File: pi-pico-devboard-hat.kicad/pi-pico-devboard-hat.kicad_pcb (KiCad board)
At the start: 2 copper layers, 65 x 56 mm, 6 parts, among them J1 Conn_01x24_Male, P1 Conn_02x20_Odd_Even

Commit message: first prototype DRC error free
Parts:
- added ?: , , F.Cu at (258.2, 126.2)
- added D1: D_Schottky, Diode_THT:D_DO-41_SOD81_P7.62mm_Horizontal, F.Cu at (209.6, 109.5)
- added J2: Conn_Pico_1, Connector_PinHeader_2.54mm:PinHeader_1x20_P2.54mm_Vertical, F.Cu at (202.0, 141.3)
- added J3: Conn_SWD, Connector_PinHeader_2.54mm:PinHeader_1x03_P2.54mm_Vertical, F.Cu at (255.6, 129.4)
- added J4: Conn_Pico_2, Connector_PinHeader_2.54mm:PinHeader_1x20_P2.54mm_Vertical, F.Cu at (250.2, 113.2)
- added SW1: SW_Reset, Button_Switch_THT:SW_PUSH_6mm, F.Cu at (261.7, 110.9)
- added U1: Pico, user:RPi_Pico_SMD_TH, F.Cu at (226.1, 126.9)
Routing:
- net /GPIO15(RXD0): track 8.70 -> 60.4 mm
- net /GPIO14(TXD0): track 8.70 -> 50.8 mm, vias 0 -> 1
- net /GPIO25(GEN6): track 7.39 -> 47.7 mm
- net Net-(J4-Pad10): track 0.00 -> 40.1 mm, vias 0 -> 1
- net /GPIO24(GEN5): track 7.29 -> 45.4 mm
- net +5V: track 2.54 -> 19.6 mm
- net /VSYS: track 0.00 -> 11.4 mm
- net GND: track 10.4 -> 16.1 mm
- net Net-(J2-Pad9): track 0.00 -> 5.56 mm
- net Net-(J2-Pad7): track 0.00 -> 5.56 mm
- net Net-(J2-Pad6): track 0.00 -> 5.56 mm
- net Net-(J2-Pad5): track 0.00 -> 5.56 mm
- net Net-(J2-Pad4): track 0.00 -> 5.56 mm
- net Net-(J2-Pad20): track 0.00 -> 5.56 mm
- net Net-(J2-Pad19): track 0.00 -> 5.56 mm
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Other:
- board text added: "Reset"

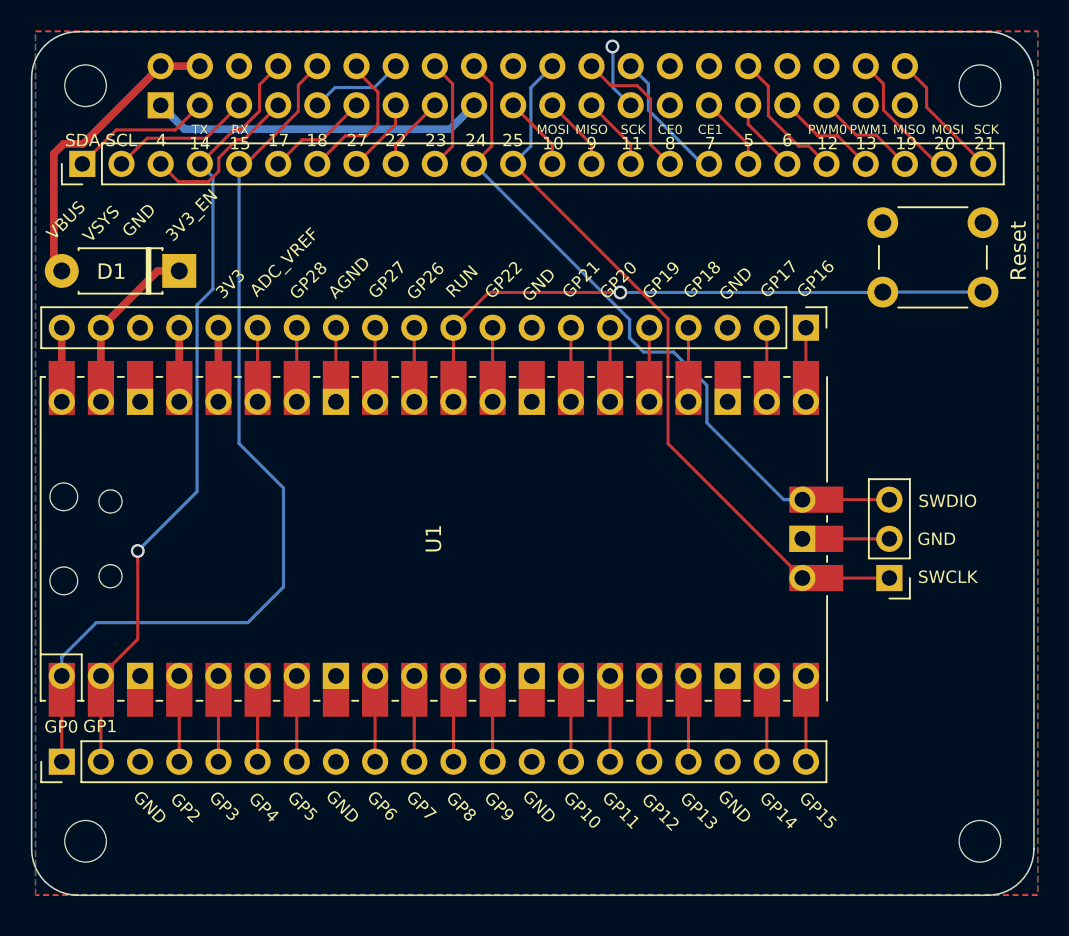
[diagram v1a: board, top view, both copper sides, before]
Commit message: Rev 2: removed unneeded connectors
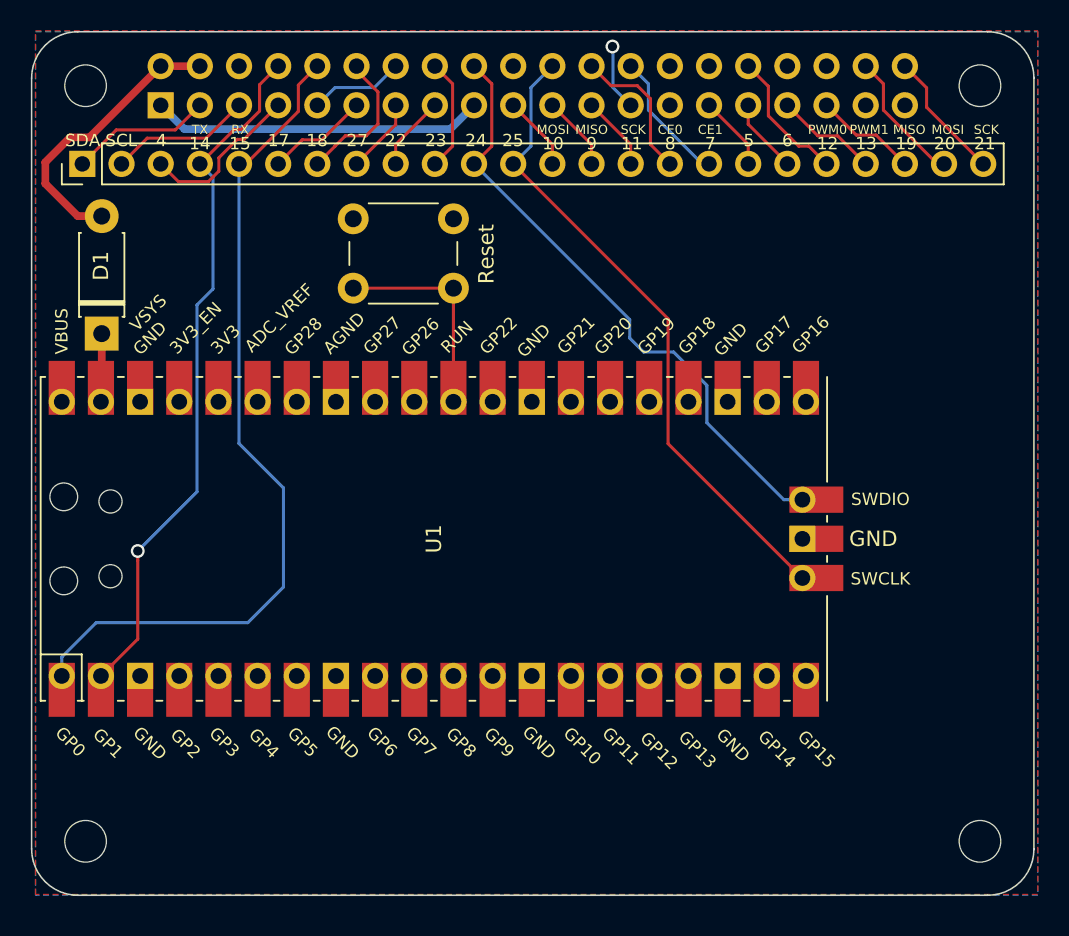
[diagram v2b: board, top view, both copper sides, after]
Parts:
- removed ?: , 
- removed J2: Conn_Pico_1, Connector_PinHeader_2.54mm:PinHeader_1x20_P2.54mm_Vertical
- removed J3: Conn_SWD, Connector_PinHeader_2.54mm:PinHeader_1x03_P2.54mm_Vertical
- removed J4: Conn_Pico_2, Connector_PinHeader_2.54mm:PinHeader_1x20_P2.54mm_Vertical
- moved SW1 34.3 mm to (227.4, 110.6)
- moved D1 6.47 mm to (204.5, 113.6), turned to 90 degrees
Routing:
- net Net-(SW1-Pad1): track 40.1 -> 13.9 mm, vias 1 -> 0
- net /VSYS: track 11.4 -> 4.44 mm
- net /GPIO25(GEN6): track 47.7 -> 42.0 mm
- net /GPIO24(GEN5): track 45.4 -> 39.7 mm
- net GND: track 16.1 -> 10.4 mm
- net Net-(U1-Pad9): track 5.56 -> 0.00 mm
- net Net-(U1-Pad7): track 5.56 -> 0.00 mm
- net Net-(U1-Pad6): track 5.56 -> 0.00 mm
- net Net-(U1-Pad5): track 5.56 -> 0.00 mm
- net Net-(U1-Pad4): track 5.56 -> 0.00 mm
- net Net-(U1-Pad20): track 5.56 -> 0.00 mm
- net Net-(U1-Pad19): track 5.56 -> 0.00 mm
- net Net-(U1-Pad17): track 5.56 -> 0.00 mm
- net Net-(U1-Pad16): track 5.56 -> 0.00 mm
- net Net-(U1-Pad15): track 5.56 -> 0.00 mm
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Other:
- board text added: "GND"
- board text added: "Rev: 2"
- board text added: "https://github.com/bablokb/pi-pico-devboard-hat"

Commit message: Rev 3: added IC-connector with optional pullups
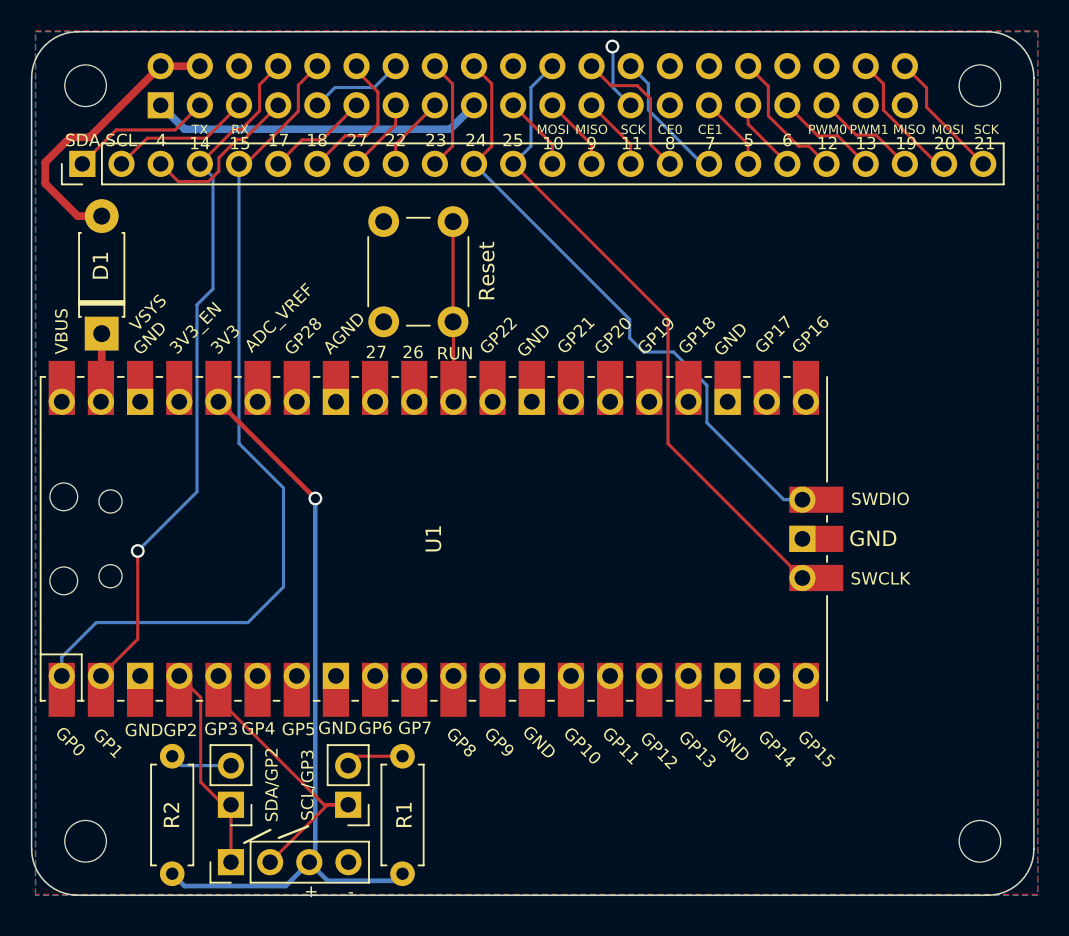
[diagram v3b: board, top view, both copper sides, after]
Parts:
- added J2: I2C, Connector_PinHeader_2.54mm:PinHeader_1x04_P2.54mm_Vertical, F.Cu at (212.9, 147.9)
- added J3: SDA_UP, Connector_PinHeader_2.54mm:PinHeader_1x02_P2.54mm_Vertical, F.Cu at (220.5, 144.1)
- added J4: SCL_UP, Connector_PinHeader_2.54mm:PinHeader_1x02_P2.54mm_Vertical, F.Cu at (212.9, 144.1)
- added R1: 4K7, Resistor_THT:R_Axial_DIN0207_L6.3mm_D2.5mm_P7.62mm_Horizontal, F.Cu at (224.1, 148.6)
- added R2: 4K7, Resistor_THT:R_Axial_DIN0207_L6.3mm_D2.5mm_P7.62mm_Horizontal, F.Cu at (209.1, 148.6)
- moved SW1 4.32 mm to (227.3, 106.3), turned to 270 degrees
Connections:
- U1 pad 4: Net-(U1-Pad4) -> /SDA_GP2
- U1 pad 5: Net-(U1-Pad5) -> /SCL_GP3
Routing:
- net /3V3: track 0.00 -> 49.2 mm, vias 0 -> 1
- net /SCL_GP3: track 0.00 -> 19.4 mm
- net /SDA_GP2: track 0.00 -> 13.8 mm
- net Net-(J4-Pad2): track 0.00 -> 4.06 mm
- net Net-(J3-Pad2): track 0.00 -> 3.78 mm
- net Net-(SW1-Pad1): track 13.9 -> 11.7 mm
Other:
- net class 3V3 added: clearance 0.2, trace_width 0.3, via_dia 0.9, via_drill 0.6
- board text added: "+"
- board text added: "-"
- board text added: "Rev: 3"
- board text added: "SCL/GP3"
- board text added: "SDA/GP2"
- board text removed: "Rev: 2"

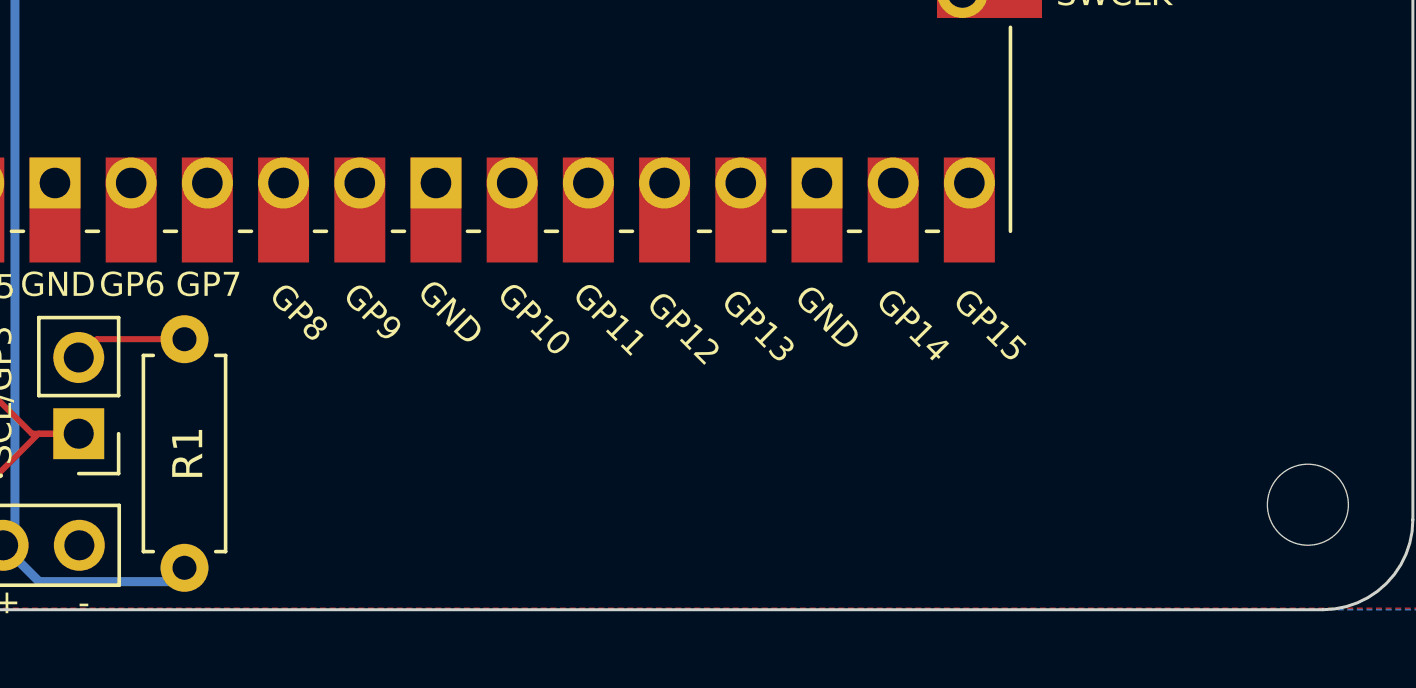
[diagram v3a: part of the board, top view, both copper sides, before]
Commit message: Rev 4: added SPI1-connector
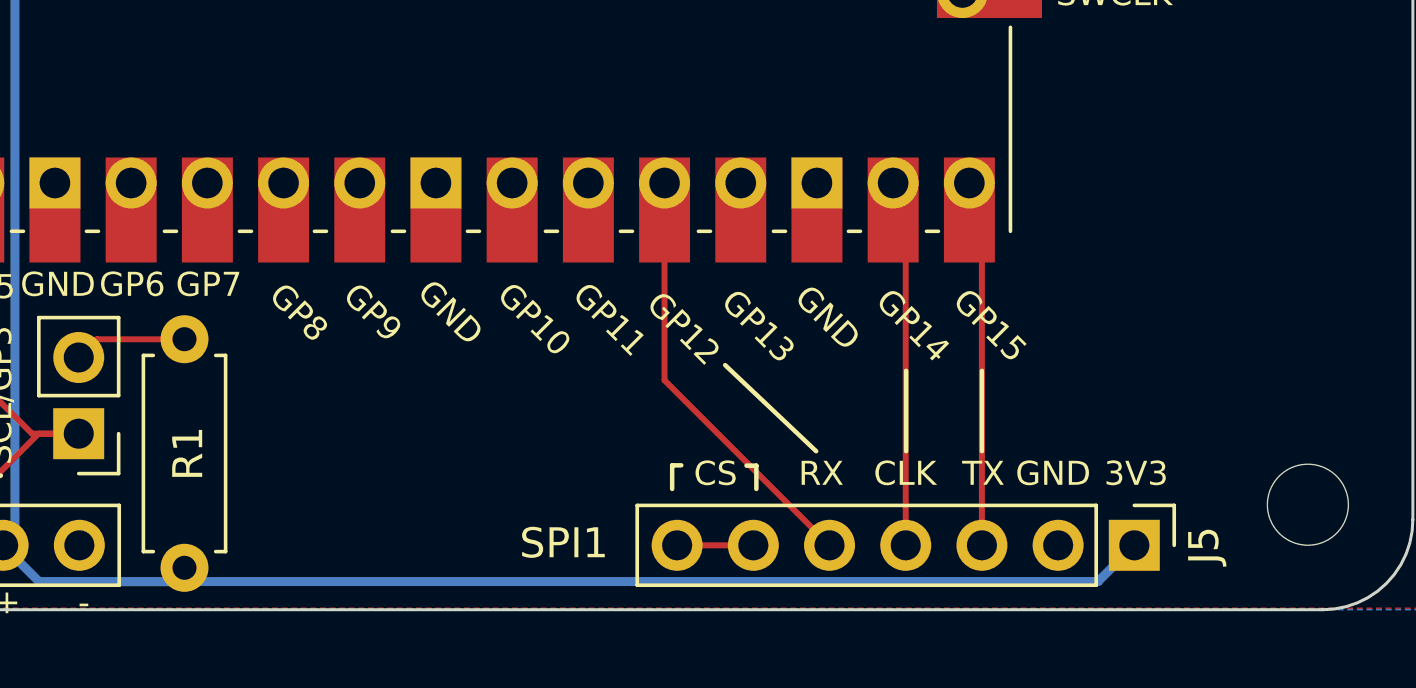
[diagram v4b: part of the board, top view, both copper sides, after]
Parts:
- added J5: Conn_SPI, Connector_PinHeader_2.54mm:PinHeader_1x07_P2.54mm_Vertical, F.Cu at (255.7, 147.9)
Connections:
- U1 pad 16: Net-(U1-Pad16) -> /SPI_RX_GP12
- U1 pad 19: Net-(U1-Pad19) -> /SPI1_CLK_GP14
- U1 pad 20: Net-(U1-Pad20) -> /SPI1TX_GP15
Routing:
- net /3V3: track 49.2 -> 81.6 mm
- net /SPI_RX_GP12: track 0.00 -> 14.4 mm
- net /SPI1_CLK_GP14: track 0.00 -> 12.3 mm
- net /SPI1TX_GP15: track 0.00 -> 12.3 mm
- net Net-(J5-Pad6): track 0.00 -> 2.54 mm
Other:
- board text added: "3V3"
- board text added: "CLK"
- board text added: "CS"
- board text added: "Rev: 4"
- board text added: "SPI1"
- board text removed: "Rev: 3"

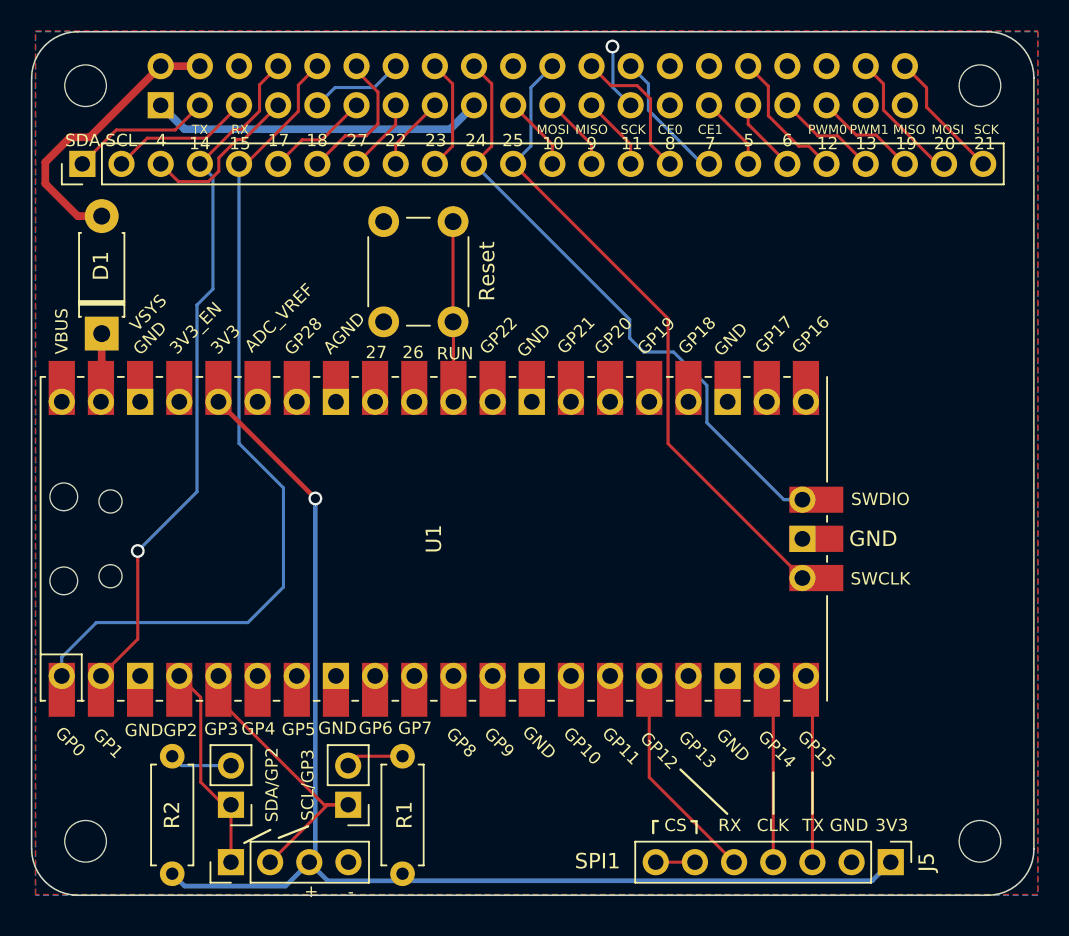
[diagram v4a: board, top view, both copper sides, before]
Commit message: Rev 5: added external connector
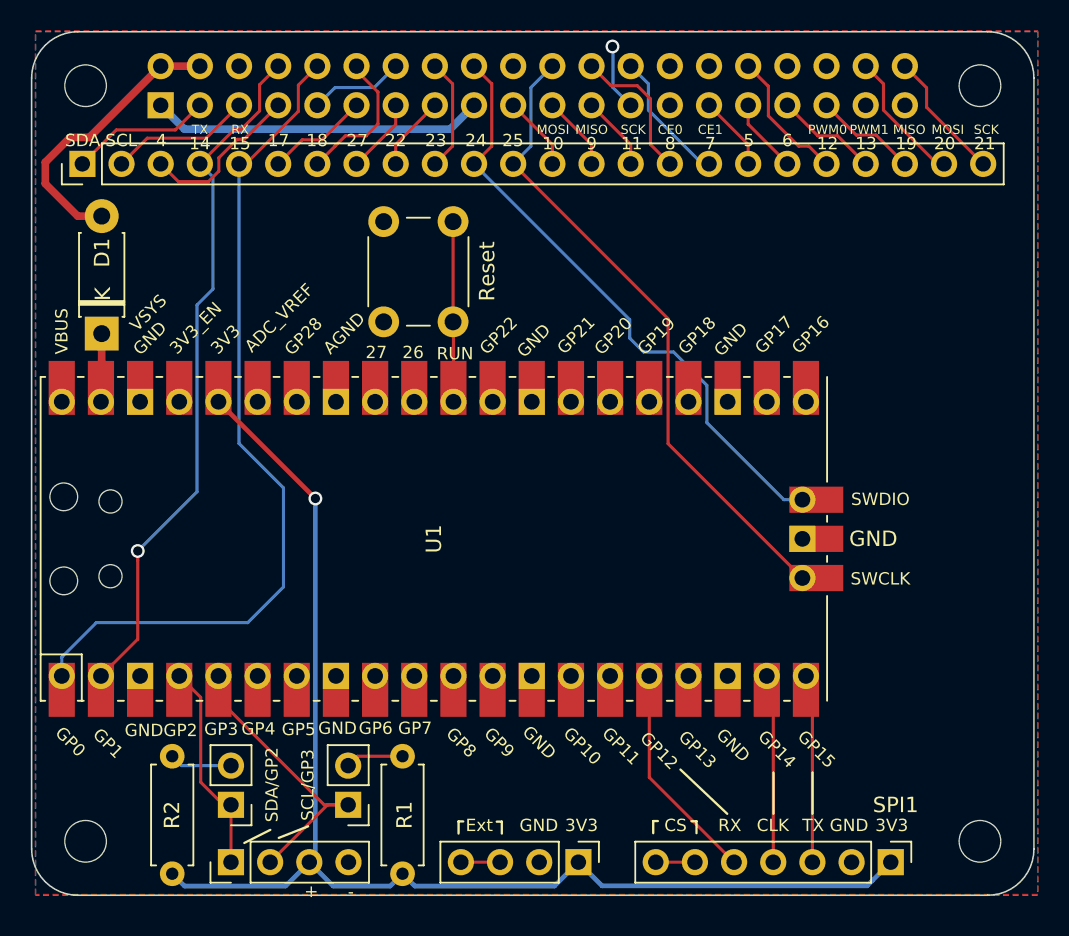
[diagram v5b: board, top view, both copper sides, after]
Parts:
- added J6: Conn_Ext, Connector_PinHeader_2.54mm:PinHeader_1x04_P2.54mm_Vertical, F.Cu at (235.5, 147.9)
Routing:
- net /3V3: track 81.6 -> 84.7 mm
- net Net-(J6-Pad3): track 0.00 -> 2.54 mm
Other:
- board text added: "Ext"
- board text added: "Rev: 5"
- board text removed: "Rev: 4"
